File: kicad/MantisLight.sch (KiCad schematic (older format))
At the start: 33 parts, among them IC1 ATMEGA32-A, K1 SPI, K3 Vin12V, P1 IMP, P2 PB2, P3 PC7, P4 PC6, P5 PORTA, P6 JTAG, P8 AREF, P9 BUTTON, U2 TSL2561, U5 7805, X1 16 MHz

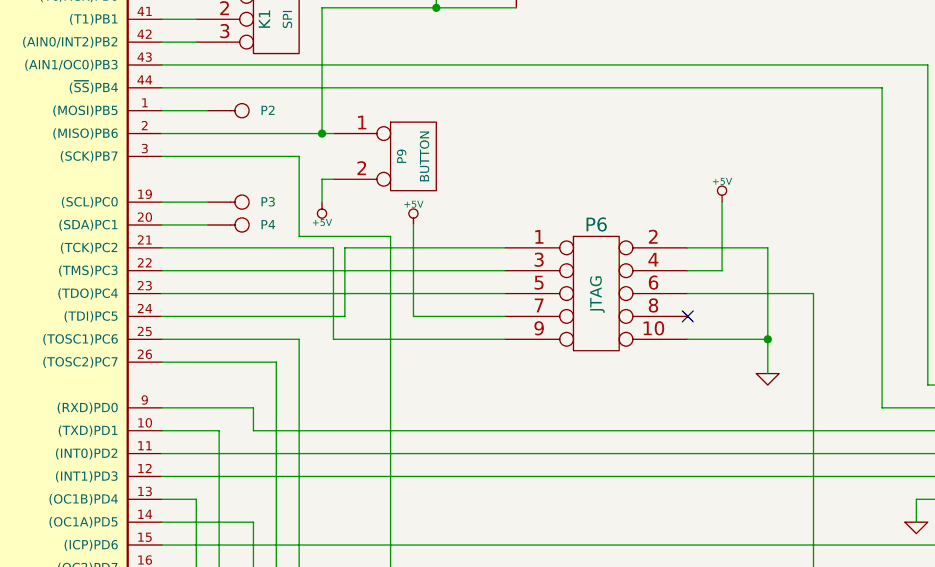
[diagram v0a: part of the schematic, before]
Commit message: fix in Schematic which did not fit the layout
JTAG Connector wiring in Schematic was wrong.
(How the hell did that happen?
Guess: Tried to "Clean" the wiring in Schematics but did not update netlist)
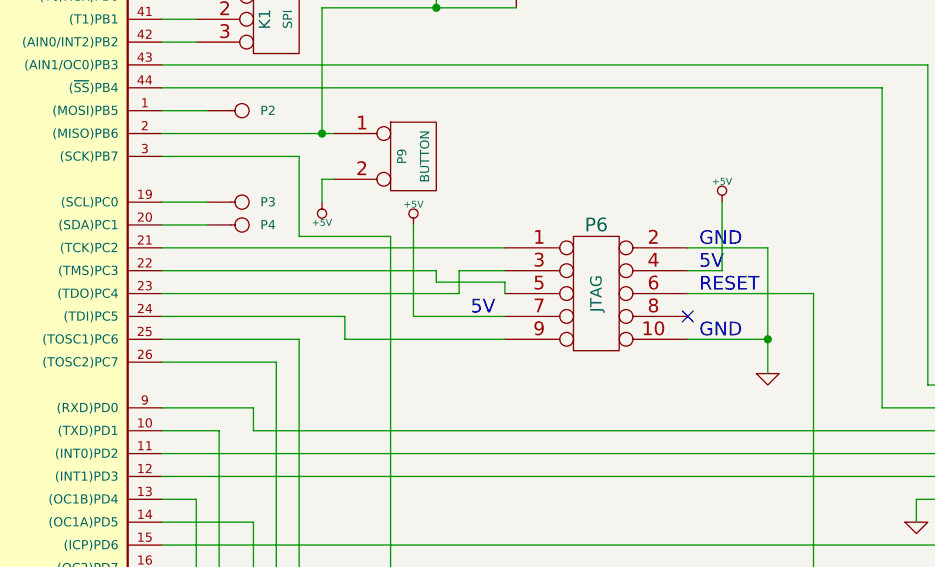
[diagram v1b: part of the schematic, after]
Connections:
- wire segments 166 -> 169
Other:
- note added: "5V"
- note added: "5V\n"
- note added: "GND"
- note added: "GND\n"
- note added: "RESET"
